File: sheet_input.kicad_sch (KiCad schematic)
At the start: 23 parts, among them J1 NCJ6FI-H, J5 VDD_PoE / PGND, Q1 DMP3098 (P-FET 60V)

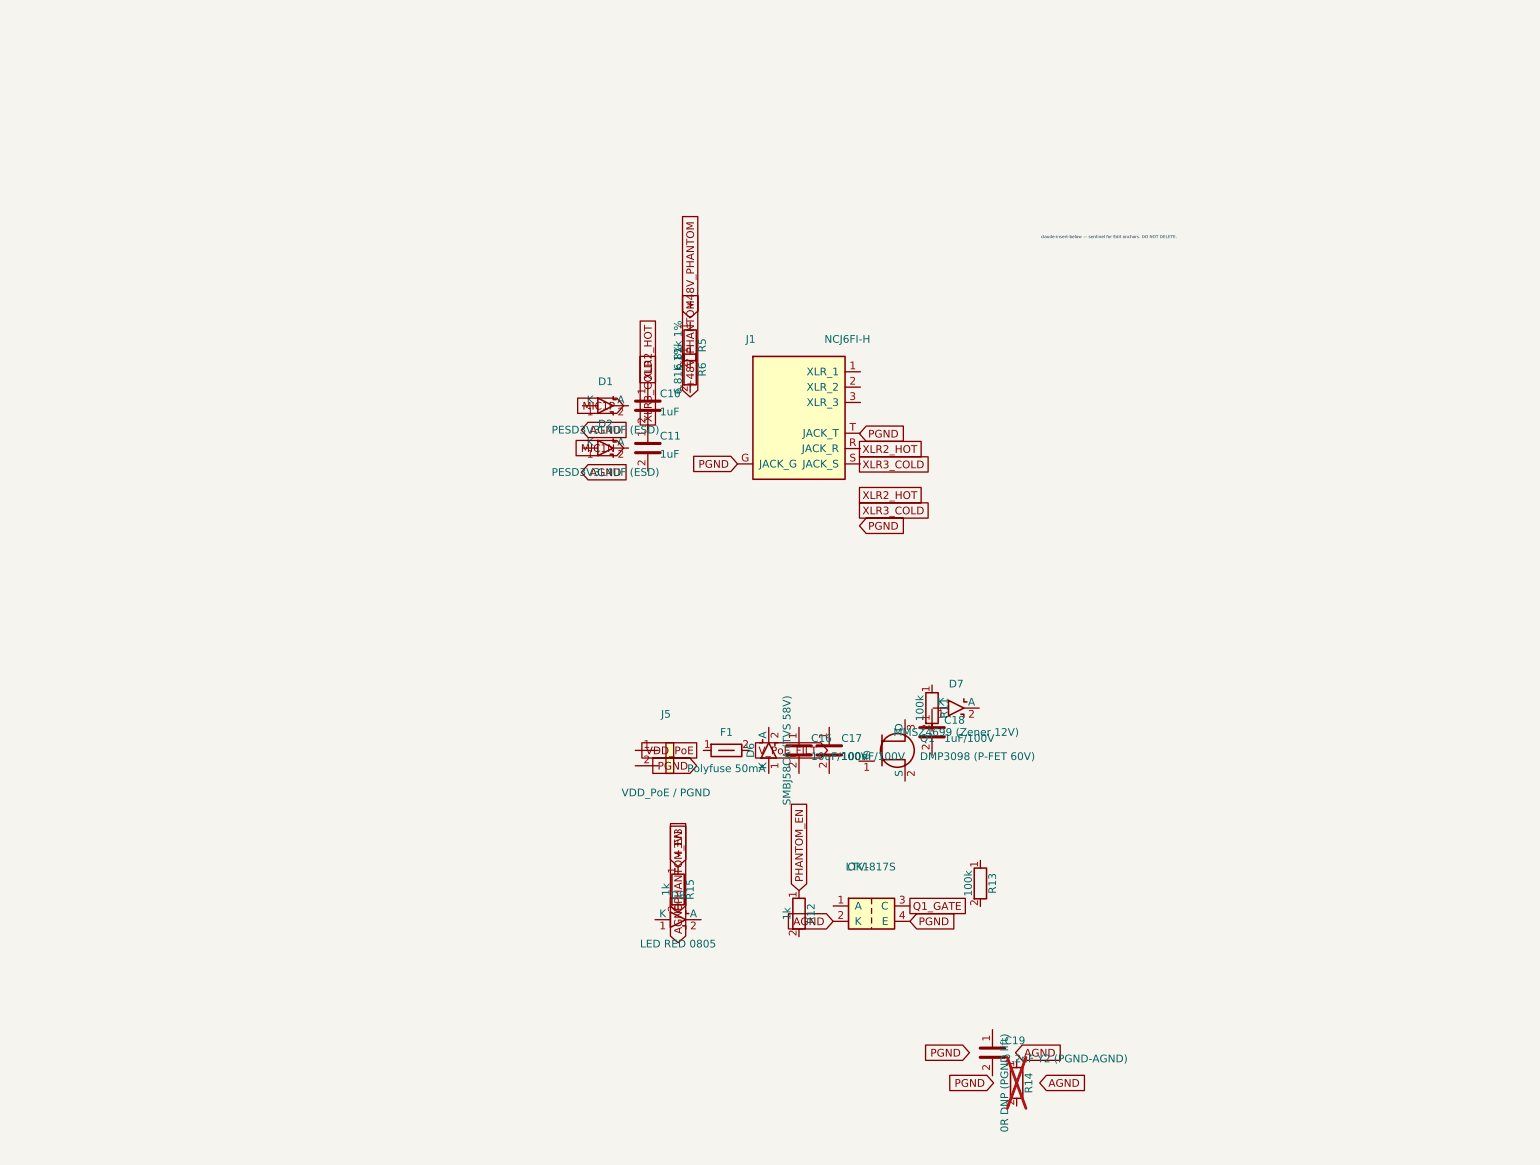
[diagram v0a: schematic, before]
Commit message: design: full iteration since init — codec, phantom/PoE, LDO, BOM, fab
First substantive commit since init; captures the entire design
iteration and quiets KiCad churn in-repo.

Codec / PCB
- ES8389: custom QFN-24 0.35mm land pattern (ES8389_QFN24_P0.35mm)
- Corrected mirror-reversed codec I2C/I2S pins
- Un-mirrored all B.Cu footprints that imported un-flipped
  (U1, OK1, Q1, D2, D6-D8 + silk)
- Re-coupled schematic to PCB netlist -> IN SYNC

Phantom / PoE
- F1 -> 1812L010/60DR (100mA hold / 60V, true 1812)
- Q1 -> Si2325DS (150V) for PoE++ margin
- Added SW1 SS-12D00-G3 slide switch = manual phantom enable (frees GPIO15)
- D8/R15/R16 phantom-present LED rework
- Confirmed PoE tap: BD1/BD2 (MB10F) -> VDD/VSS -> J5 pin 1/2

Power / connectors
- Added low-noise analog LDO U2 TPS7A2033 (+C21/C22): +5V -> +3V3_A -> AVDD
- J1 -> Neutrik NCJ6FA-H switched combo (+ 3D model)

Project
- BOM: single source of truth BOM.csv (JLCPCB-uploadable); removed BOM.md
- Added fab/ outputs (gerbers, drill, CPL) and tools/ (check_sync.py, relabel_sch.py)
- .gitignore: ignore KiCad churn (*.kicad_prl, *-drc.rpt, *-erc.rpt, backups) + local docs
- Untrack scramble_hat-erc.rpt (now ignored)
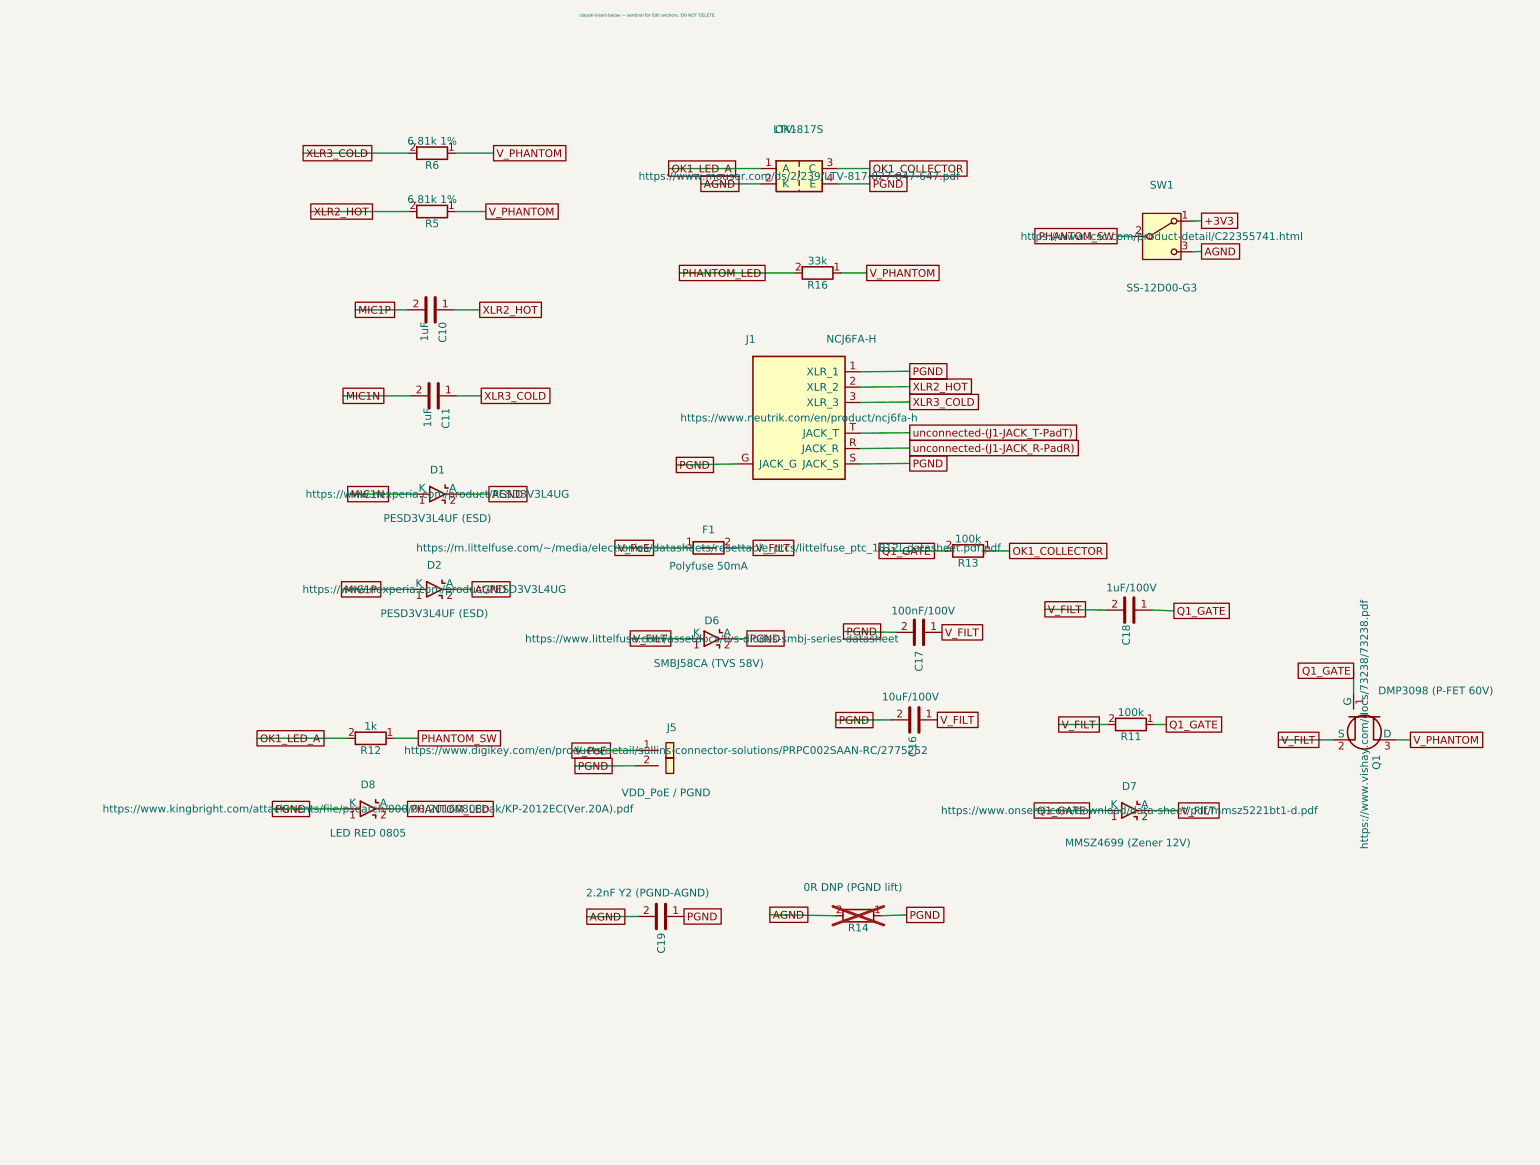
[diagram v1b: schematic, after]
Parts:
- removed R15: 1k, Resistor_SMD:R_0402_1005Metric, symbol scramble_hat:R
- added R16: 33k, Resistor_SMD:R_0805_2012Metric, symbol scramble_hat:R
- added SW1: SS-12D00-G3, scramble_hat:SW_Slide_SS-12D00-G3, symbol scramble_hat:SW_SPDT
- J1: value NCJ6FI-H -> NCJ6FA-H; footprint Connector_Audio:Jack_XLR-6.35mm_Neutrik_NCJ6FI-H_Horizontal -> Connector_Audio:Jack_XLR-6.35mm_Neutrik_NCJ6FA-H_Horizontal
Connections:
- net +3V3: now also SW1.1 (A)
- net AGND: now also C19.2, D1.2 (A), D2.2 (A), R14.2, SW1.3 (C)
- net MIC1N: now also C11.2, D1.1 (K)
- net MIC1P: now also C10.2, D2.1 (K)
- net PGND: now also C16.2, C17.2, C19.1, D6.2 (A), D8.1 (K), J1.1 (XLR_1), J1.S (JACK_S), J5.2 (Pin_2), R14.1
- net Q1_GATE: now also C18.1, D7.1 (K), Q1.1 (G), R11.1, R13.2; no longer OK1.3 (C)
- net XLR2_HOT: now also J1.2 (XLR_2), R5.2
- net XLR3_COLD: now also J1.3 (XLR_3), R6.2
- net V_PHANTOM: now reaches R6.1
- net V_PHANTOM: now also Q1.3 (D), R5.1, R16.1
- net OK1_LED_A: now reaches R12.2
- net OK1_LED_A: now also OK1.1 (A)
- net V_FILT: now reaches Q1.2 (S)
- net V_FILT: now also C16.1, C17.1, C18.2, D6.1 (K), D7.2 (A), F1.2, R11.2
- net V_PoE: now reaches F1.1
- net V_PoE: now also J5.1 (Pin_1)
- net OK1_COLLECTOR: now reaches R13.1
- net OK1_COLLECTOR: now also OK1.3 (C)
- net PHANTOM_LED: now reaches D8.2 (A)
- net PHANTOM_LED: now also R16.2
- net unconnected-(J1-JACK_R-PadR): now reaches J1.R (JACK_R)
- net unconnected-(J1-JACK_T-PadT): now reaches J1.T (JACK_T)
- net PHANTOM_EN renamed PHANTOM_SW
- net PHANTOM_SW: now also SW1.2 (B)
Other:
- moved on the sheet: C10, C11, C16, C17, C18, C19, D1, D2, D6, D7, D8, F1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
